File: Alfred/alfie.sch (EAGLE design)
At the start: 33 parts, among them IC1 7805TV, K1 G6A-234P, K2 G6A-234P

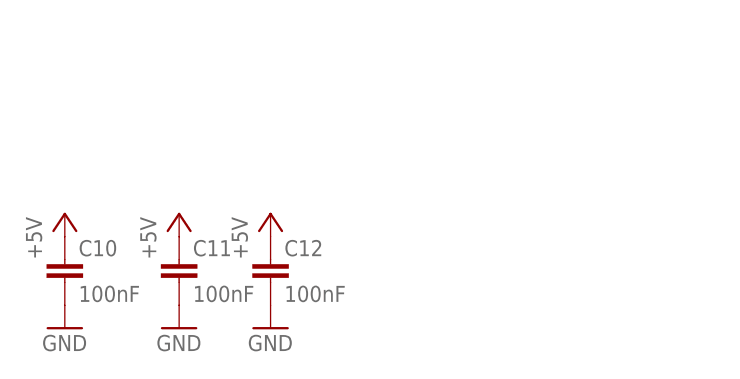
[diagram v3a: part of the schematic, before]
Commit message: Added bigass cap for relays
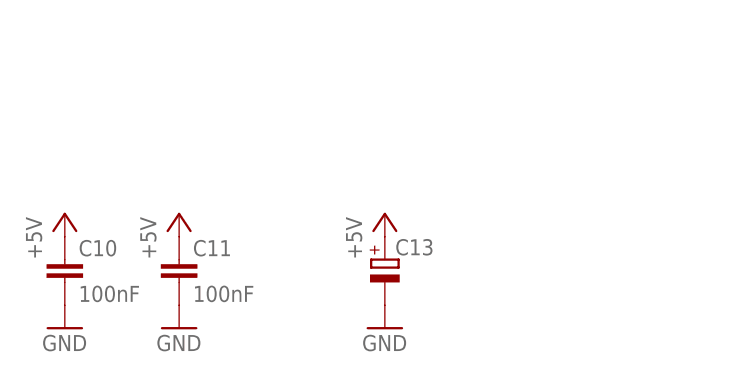
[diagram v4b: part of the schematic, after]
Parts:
- removed C12: 100nF, rcl:C-EUC0805
- added C13: (no value), rcl:CPOL-EUE5-8.5
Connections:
- net +5V: now also C13.+; no longer C12.1
- net GND: now also C13.-; no longer C12.2
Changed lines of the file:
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@@
 <part name="C10" library="rcl" deviceset="C-EU" device="C0805" value="100nF"/>
 <part name="C11" library="rcl" deviceset="C-EU" device="C0805" value="100nF"/>
-<part name="C12" library="rcl" deviceset="C-EU" device="C0805" value="100nF"/>
 <part name="GND10" library="supply1" deviceset="GND" device=""/>
 <part name="GND11" library="supply1" deviceset="GND" device=""/>
-<part name="GND12" library="supply1" deviceset="GND" device=""/>
-<part name="P+7" library="supply1" deviceset="+5V" device=""/>
 <part name="P+8" library="supply1" deviceset="+5V" device=""/>
 <part name="P+9" library="supply1" deviceset="+5V" device=""/>
 <part name="FRAME1" library="frames" deviceset="A4L-LOC" device=""/>
+<part name="C13" library="rcl" deviceset="CPOL-EU" device="E5-8.5"/>
+<part name="P+10" library="supply1" deviceset="+5V" device=""/>
+<part name="GND13" library="supply1" deviceset="GND" device=""/>
 </parts>
 <sheets>
@@
 <instance part="C10" gate="G$1" x="-35.56" y="-58.42"/>
 <instance part="C11" gate="G$1" x="-22.86" y="-58.42"/>
-<instance part="C12" gate="G$1" x="-12.7" y="-58.42"/>
 <instance part="GND10" gate="1" x="-35.56" y="-66.04"/>
 <instance part="GND11" gate="1" x="-22.86" y="-66.04"/>
-<instance part="GND12" gate="1" x="-12.7" y="-66.04"/>
-<instance part="P+7" gate="1" x="-12.7" y="-53.34"/>
 <instance part="P+8" gate="1" x="-22.86" y="-53.34"/>
 <instance part="P+9" gate="1" x="-35.56" y="-53.34"/>
 <instance part="FRAME1" gate="G$1" x="-48.26" y="-78.74"/>
+<instance part="C13" gate="G$1" x="0" y="-58.42"/>
+<instance part="P+10" gate="1" x="0" y="-53.34"/>
+<instance part="GND13" gate="1" x="0" y="-66.04"/>
 </instances>
 <busses>
@@
 </segment>
 <segment>
-<pinref part="C12" gate="G$1" pin="1"/>
-<pinref part="P+7" gate="1" pin="+5V"/>
-</segment>
-<segment>
 <pinref part="C11" gate="G$1" pin="1"/>
 <pinref part="P+8" gate="1" pin="+5V"/>
@@
 <pinref part="C10" gate="G$1" pin="1"/>
 <pinref part="P+9" gate="1" pin="+5V"/>
+</segment>
+<segment>
+<pinref part="C13" gate="G$1" pin="+"/>
+<pinref part="P+10" gate="1" pin="+5V"/>
 </segment>
 </net>
@@
 </segment>
 <segment>
-<pinref part="C12" gate="G$1" pin="2"/>
-<pinref part="GND12" gate="1" pin="GND"/>
+<pinref part="C13" gate="G$1" pin="-"/>
+<pinref part="GND13" gate="1" pin="GND"/>
 </segment>
 </net>

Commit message: Applied bjdooks patches to bring this to the board as etched.
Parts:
- removed K2: G6A-234P, relay:G6A-234P
- added K3: 4052, relay:4052
- K1: value G6A-234P -> 4052; device relay:G6A-234P -> relay:4052; OC_FARNELL (none) -> unknown; OC_NEWARK (none) -> unknown
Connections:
- removed net N$7: K22.P, X3-2.KL
- new net N$6: K33.S, X3-2.KL
- net +5V: now also K11.2, K31.2; no longer K11.1, K21.1
- net N$1: now also K11.1; no longer K11.2
- net N$2: now also K31.1; no longer K21.2
- net N$4: now also K33.P; no longer K22.S
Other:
- moved on the sheet: C1, C10, C11, C13, C2, D1, D2, D3, D4, D5, D6, IC1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
